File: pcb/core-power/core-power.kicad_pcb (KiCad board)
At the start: 2 copper layers, 28.6 x 34.7 mm, 24 parts, among them J1 USB_C_Receptacle_USB2.0_16P, J2 USB_C_Receptacle_USB2.0_16P, J3 Screw_Terminal_01x05, U1 INA226, U2 INA226, U3 INA226, U4 TUSB320, U5 TUSB320, U6 MCP130T-315I/SN, U7 TPS2121RUXR

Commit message: Various things were completed
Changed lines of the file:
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@@
 			(at 0 -2.85 0)
 			(layer "F.SilkS")
+			(hide yes)
 			(effects
 				(font

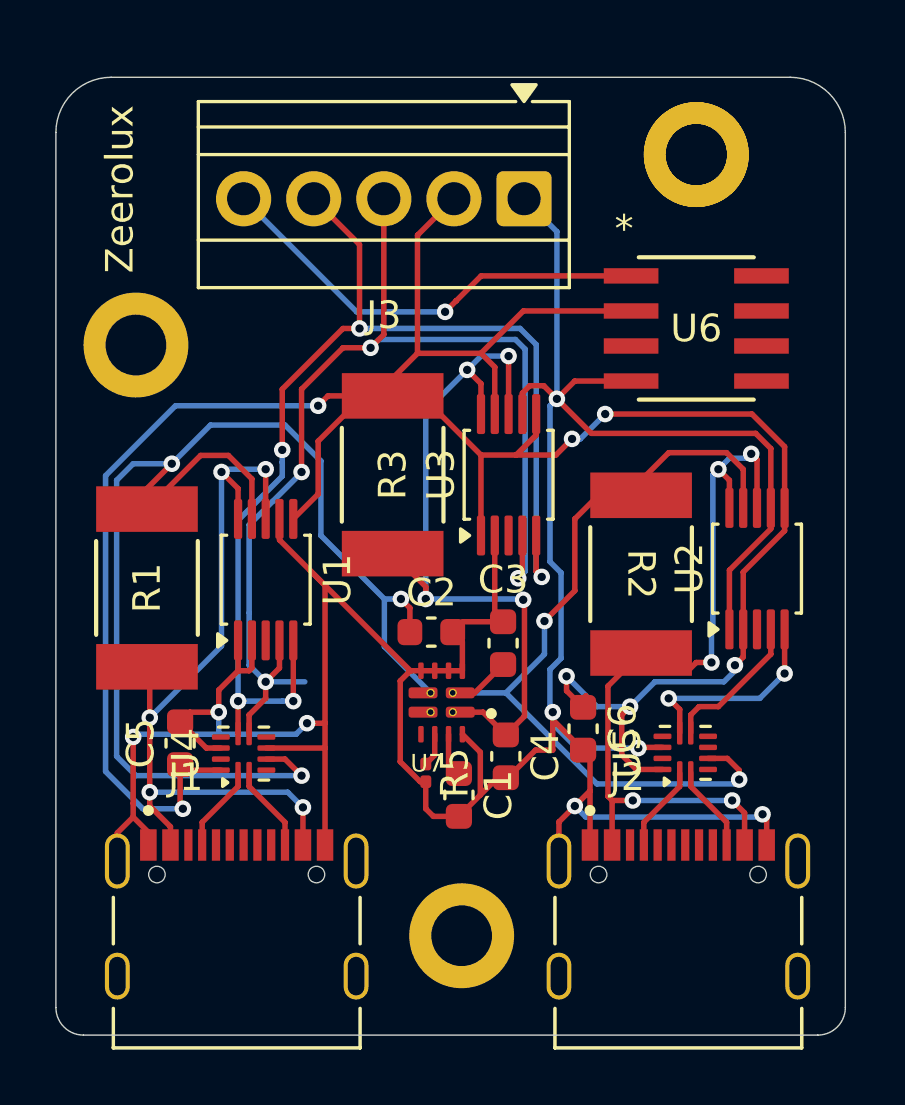
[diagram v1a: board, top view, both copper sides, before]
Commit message: added bom
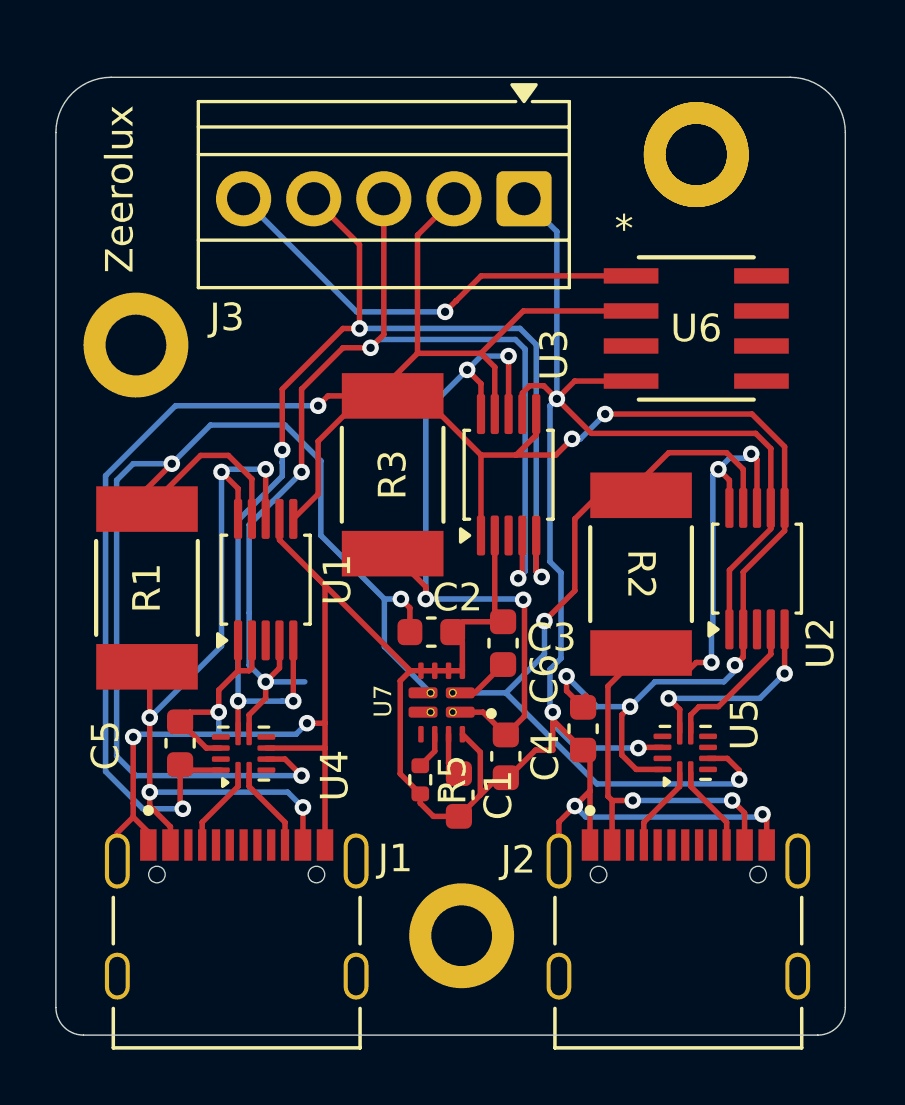
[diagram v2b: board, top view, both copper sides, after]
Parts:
- R5: footprint Resistor_SMD:R_0201_0603Metric -> Resistor_SMD:R_0402_1005Metric
- moved R5 0.32 mm to (89.9, 118.5)
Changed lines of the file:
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@@
 			(outputformat 1)
 			(mirror no)
-			(drillshape 1)
+			(drillshape 0)
 			(scaleselection 1)
-			(outputdirectory "")
+			(outputdirectory "core-power-gerber/")
 		)
 	)
@@
 		(tags "capacitor")
 		(property "Reference" "C3"
-			(at 2.3 0 180)
+			(at 0.2 1.75 180)
 			(layer "F.SilkS")
 			(effects
@@
 		(tags "Texas X2QFN NoLead")
 		(property "Reference" "U5"
-			(at 0 -2.1 90)
+			(at 1.025 2.15 90)
 			(layer "F.SilkS")
 			(effects
@@
 		(tags "VSSOP SO")
 		(property "Reference" "U3"
-			(at 0 -2.45 90)
+			(at 4.35 1.65 90)
 			(layer "F.SilkS")
 			(effects
@@
 		(tags "THT Terminal Block Xinya XY308-2.54-5P pitch 2.54mm size 13.2x6.5mm drill 1.2mm pad 2mm")
 		(property "Reference" "J3"
-			(at 5.08 -4.22 0)
+			(at 10.76 -4.3 0)
 			(layer "F.SilkS")
 			(effects
@@
 		(tags "capacitor")
 		(property "Reference" "C6"
-			(at 0 -1.43 90)
+			(at -1.8 1.4 90)
 			(layer "F.SilkS")
 			(effects
@@
 		(at 83.25 125.6625)
 		(property "Reference" "J1"
-			(at -1.85 -7.205 0)
+			(at 5.75 -4.2625 0)
 			(layer "F.SilkS")
 			(effects
@@
 		(tags "VSSOP SO")
 		(property "Reference" "U2"
-			(at 0 -2.45 90)
+			(at -2.7 2.3 90)
 			(layer "F.SilkS")
 			(effects
@@
 		(tags "capacitor")
 		(property "Reference" "C2"
-			(at 0 -1.43 0)
+			(at 0.95 -1.25 0)
 			(layer "F.SilkS")
 			(effects
@@
 		)
 	)
-	(footprint "Resistor_SMD:R_0201_0603Metric"
+	(footprint "Resistor_SMD:R_0402_1005Metric"
 		(layer "F.Cu")
-		(at 90.1 118.3 -90)
-		(descr "Resistor SMD 0201 (0603 Metric), square (rectangular) end terminal, IPC-7351 nominal, (Body size source: https://www.vishay.com/docs/20052/crcw0201e3.pdf), generated with kicad-footprint-generator")
+		(at 89.9 118.55 -90)
+		(descr "Resistor SMD 0402 (1005 Metric), square (rectangular) end terminal, IPC-7351 nominal, (Body size source: IPC-SM-782 page 72, https://www.pcb-3d.com/wordpress/wp-content/uploads/ipc-sm-782a_amendment_1_and_2.pdf), generated with kicad-footprint-generator")
 		(tags "resistor")
 		(property "Reference" "R5"
-			(at 0 -1.05 90)
+			(at 0 -1.17 270)
 			(layer "F.SilkS")
 			(effects
@@
 		)
 		(property "Value" "5.5k"
-			(at 0 1.05 90)
+			(at 0 1.17 270)
 			(layer "F.Fab")
 			(effects
@@
 			)
 		)
-		(property "Datasheet" "~"
-			(at 0 0 90)
+		(property "Datasheet" ""
+			(at 0 0 270)
 			(layer "F.Fab")
 			(hide yes)
@@
 			)
 		)
-		(property "Description" "Resistor"
-			(at 0 0 90)
+		(property "Description" ""
+			(at 0 0 270)
 			(layer "F.Fab")
 			(hide yes)
@@
 		(attr smd)
 		(fp_line
-			(start -0.7 0.35)
-			(end -0.7 -0.35)
+			(start -0.153641 0.38)
+			(end 0.153641 0.38)
+			(stroke
+				(width 0.12)
+				(type solid)
+			)
+			(layer "F.SilkS")
+		)
+		(fp_line
+			(start -0.153641 -0.38)
+			(end 0.153641 -0.38)
+			(stroke
+				(width 0.12)
+				(type solid)
+			)
+			(layer "F.SilkS")
+		)
+		(fp_line
+			(start -0.93 0.47)
+			(end -0.93 -0.47)
 			(stroke
 				(width 0.05)
@@
 		)
 		(fp_line
-			(start 0.7 0.35)
-			(end -0.7 0.35)
+			(start 0.93 0.47)
+			(end -0.93 0.47)
 			(stroke
 				(width 0.05)
@@
 		)
 		(fp_line
-			(start -0.7 -0.35)
-			(end 0.7 -0.35)
+			(start -0.93 -0.47)
+			(end 0.93 -0.47)
 			(stroke
 				(width 0.05)
@@
 		)
 		(fp_line
-			(start 0.7 -0.35)
-			(end 0.7 0.35)
+			(start 0.93 -0.47)
+			(end 0.93 0.47)
 			(stroke
 				(width 0.05)
@@
 		)
 		(fp_line
-			(start -0.3 0.15)
-			(end -0.3 -0.15)
+			(start -0.525 0.27)
+			(end -0.525 -0.27)
 			(stroke
 				(width 0.1)
@@
 		)
 		(fp_line
-			(start 0.3 0.15)
-			(end -0.3 0.15)
+			(start 0.525 0.27)
+			(end -0.525 0.27)
 			(stroke
 				(width 0.1)
@@
 		)
 		(fp_line
-			(start -0.3 -0.15)
-			(end 0.3 -0.15)
+			(start -0.525 -0.27)
+			(end 0.525 -0.27)
 			(stroke
 				(width 0.1)
@@
 		)
 		(fp_line
-			(start 0.3 -0.15)
-			(end 0.3 0.15)
+			(start 0.525 -0.27)
+			(end 0.525 0.27)
 			(stroke
 				(width 0.1)
@@
 		)
 		(fp_text user "${REFERENCE}"
-			(at 0 -0.68 90)
+			(at 0 0 270)
 			(layer "F.Fab")
 			(effects
 				(font
-					(size 0.25 0.25)
+					(size 0.26 0.26)
 					(thickness 0.04)
 				)
 			)
 		)
-		(pad "" smd roundrect
-			(at -0.345 0 270)
-			(size 0.318 0.36)
-			(layers "F.Paste")
-			(roundrect_rratio 0.25)
-		)
-		(pad "" smd roundrect
-			(at 0.345 0 270)
-			(size 0.318 0.36)
-			(layers "F.Paste")
-			(roundrect_rratio 0.25)
-		)
 		(pad "1" smd roundrect
-			(at -0.32 0 270)
-			(size 0.46 0.4)
-			(layers "F.Cu" "F.Mask")
+			(at -0.51 0 270)
+			(size 0.54 0.64)
+			(layers "F.Cu" "F.Mask" "F.Paste")
 			(roundrect_rratio 0.25)
 			(net 28 "Net-(U7-ILIM)")
@@
 		)
 		(pad "2" smd roundrect
-			(at 0.32 0 270)
-			(size 0.46 0.4)
-			(layers "F.Cu" "F.Mask")
+			(at 0.51 0 270)
+			(size 0.54 0.64)
+			(layers "F.Cu" "F.Mask" "F.Paste")
 			(roundrect_rratio 0.25)
 			(net 2 "GND")
@@
 		)
 		(embedded_fonts no)
-		(model "${KICAD9_3DMODEL_DIR}/Resistor_SMD.3dshapes/R_0201_0603Metric.step"
+		(model "${KICAD9_3DMODEL_DIR}/Resistor_SMD.3dshapes/R_0402_1005Metric.step"
 			(offset
 				(xyz 0 0 0)
@@
 		(at 99.25 125.6625)
 		(property "Reference" "J2"
-			(at -1.85 -7.205 0)
+			(at -5.8 -4.2125 0)
 			(layer "F.SilkS")
 			(effects
@@
 		(tags "Texas X2QFN NoLead")
 		(property "Reference" "U4"
-			(at 0 -2.1 90)
+			(at -0.8 3.3 90)
 			(layer "F.SilkS")
 			(effects
@@
 		(at 90.675 115.75 180)
 		(property "Reference" "U7"
-			(at 0.532 -2.2064 0)
+			(at 2.125 0.05 270)
 			(layer "F.SilkS")
 			(effects
@@
 		(tags "capacitor")
 		(property "Reference" "C5"
-			(at 0 -1.43 90)
+			(at -0.075 -2.7 90)
 			(layer "F.SilkS")
 			(effects
@@
 	)
 	(segment
-		(start 89.174 114.967176)
-		(end 89.541176 114.6)
-		(width 0.2)
-		(layer "F.Cu")
-		(net 2)
-	)
-	(segment
 		(start 83.8 114.5)
 		(end 83.8 113.5)
@@
 	)
 	(segment
-		(start 91.3 119.875)
-		(end 90.375 119.875)
-		(width 0.2)
-		(layer "F.Cu")
-		(net 2)
-	)
-	(segment
-		(start 89.900001 118.62)
-		(end 89.174 117.893999)
+		(start 89.9 119.06)
+		(end 89.9 119.4)
 		(width 0.2)
 		(layer "F.Cu")
@@
 	)
 	(segment
-		(start 90.1 119.6)
-		(end 90.1 118.62)
+		(start 86.45 117.4)
+		(end 86.45 116.5)
 		(width 0.2)
 		(layer "F.Cu")
@@
 	)
 	(segment
-		(start 86.45 117.4)
-		(end 86.45 116.5)
+		(start 92.6 112.525)
+		(end 92.9 112.825)
 		(width 0.2)
 		(layer "F.Cu")
@@
 	)
 	(segment
-		(start 92.6 112.525)
-		(end 92.9 112.825)
+		(start 89.541176 114.6)
+		(end 89.174 114.967176)
 		(width 0.2)
 		(layer "F.Cu")
@@
 	)
 	(segment
-		(start 93 118.475)
-		(end 93.075 118.475)
+		(start 89.174 114.967176)
+		(end 89.174 118.334)
 		(width 0.2)
 		(layer "F.Cu")
@@
 	)
 	(segment
-		(start 79.5 119.4)
-		(end 79.5 117)
+		(start 93 118.475)
+		(end 93.075 118.475)
 		(width 0.2)
 		(layer "F.Cu")
@@
 	)
 	(segment
-		(start 90.375 119.875)
-		(end 90.1 119.6)
+		(start 79.5 119.4)
+		(end 79.5 117)
 		(width 0.2)
 		(layer "F.Cu")
@@
 	)
 	(segment
+		(start 90.375 119.875)
+		(end 91.3 119.875)
+		(width 0.2)
+		(layer "F.Cu")
+		(net 2)
+	)
+	(segment
 		(start 101.1 113.1)
 		(end 101.1 110.958824)
@@
 	)
 	(segment
-		(start 94.925 120.075)
-		(end 95.5 119.5)
+		(start 89.174 118.334)
+		(end 89.9 119.06)
 		(width 0.2)
 		(layer "F.Cu")
@@
 	)
 	(segment
-		(start 90.1 118.62)
-		(end 89.900001 118.62)
+		(start 94.925 120.075)
+		(end 95.5 119.5)
 		(width 0.2)
 		(layer "F.Cu")
@@
 	)
 	(segment
-		(start 89.174 117.893999)
-		(end 89.174 114.967176)
-		(width 0.2)
-		(layer "F.Cu")
-		(net 2)
-	)
-	(segment
 		(start 102.6 109.458824)
 		(end 102.6 108.7)
@@
 		(net 2)
 	)
+	(segment
+		(start 89.9 119.4)
+		(end 90.375 119.875)
+		(width 0.2)
+		(layer "F.Cu")
+		(net 2)
+	)
 	(via
 		(at 97.8 117.4)
@@
 	)
 	(segment
-		(start 90.425 116.9)
-		(end 90.425 117.655)
+		(start 90.425 117.515)
+		(end 89.9 118.04)
 		(width 0.2)
 		(layer "F.Cu")
@@
 	)
 	(segment
-		(start 90.425 117.655)
-		(end 90.1 117.98)
+		(start 90.425 116.9)
+		(end 90.425 117.515)
 		(width 0.2)
 		(layer "F.Cu")
